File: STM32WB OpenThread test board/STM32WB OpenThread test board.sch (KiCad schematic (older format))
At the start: 0 parts

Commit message: Introduce MCU
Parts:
- added C?: 100n, symbol Device:C_Polarized
- added C? (x8): C, symbol Device:C
- added C?: 100n, symbol Device:C
- added J?: Conn_Coaxial, symbol Connector:Conn_Coaxial
- added L?: L, symbol Device:L
- added SW?: SW_Push, symbol Switch:SW_Push
- added U?: STM32WB15CC, Package_DFN_QFN:QFN-48-1EP_7x7mm_P0.5mm_EP5.6x5.6mm, symbol MCU_ST_STM32WB:STM32WB15CC
- added Y?: 32MHz, symbol Device:Crystal
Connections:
- new net: U?.24 (OSC_OUT), Y?.1
- new net: U?.25 (OSC_IN), Y?.2
- new net: C?.2, L?.2, U?.31 (VFBSMPS)
- new net: L?.1, U?.33 (VLXSMPS)
- new net: C?.1, SW?.2, U?.7 (NRST)
- new net GND: C?.1, C?.2, C?.2, J?.2 (Ext), SW?.1, U?.22 (VSSRF), U?.32 (VSSSMPS), U?.49 (VSS)
- new net VDD: C?.1, U?.1 (VBAT), U?.20 (VDD), U?.23 (VDDRF), U?.34 (VDDSMPS), U?.35 (VDD), U?.40 (VDD), U?.48 (VDD), U?.8 (VDDA)
- no-connect marks 0 -> 2
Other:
- note added: "RF"

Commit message: WIP
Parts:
- added C? (x2): C, symbol Device:C
- added R?: R, symbol Device:R
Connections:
- net GND: now also C?.1, C?.1, C?.1; no longer C?.2
- net VDD: now also R?.1
- net at U?.24 (OSC_OUT): now also Y?.2, C?.2; no longer Y?.1
- net at U?.25 (OSC_IN): now also Y?.1, C?.2; no longer Y?.2
- net at SW?.2, U?.7 (NRST): now also C?.2, R?.2; no longer C?.1
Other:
- moved on the sheet: C?, J?, SW?, Y?
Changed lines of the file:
@@
 L Device:Crystal Y?
 U 1 1 6229DF59
-P 4450 1750
-F 0 "Y?" H 4450 1482 50  0000 C CNN
-F 1 "32MHz" H 4450 1573 50  0000 C CNN
-F 2 "" H 4450 1750 50  0001 C CNN
-F 3 "~" H 4450 1750 50  0001 C CNN
-	1    4450 1750
-	-1   0    0    1
-$EndComp
-Wire Wire Line
-	4600 1800 4950 1800
-Wire Wire Line
-	4950 1900 4300 1900
-Wire Wire Line
-	4600 1800 4600 1750
-Wire Wire Line
-	4300 1750 4300 1900
+P 3850 1550
+F 0 "Y?" H 3850 1282 50  0000 C CNN
+F 1 "32MHz" H 3850 1373 50  0000 C CNN
+F 2 "" H 3850 1550 50  0001 C CNN
+F 3 "~" H 3850 1550 50  0001 C CNN
+	1    3850 1550
+	1    0    0    -1
+$EndComp
 Wire Wire Line
 	5350 1400 5450 1400
@@
 L Connector:Conn_Coaxial J?
 U 1 1 622A9FE4
-P 4000 2100
-F 0 "J?" V 4237 2029 50  0000 C CNN
-F 1 "Conn_Coaxial" V 4146 2029 50  0000 C CNN
-F 2 "" H 4000 2100 50  0001 C CNN
-F 3 " ~" H 4000 2100 50  0001 C CNN
-	1    4000 2100
+P 3150 2100
+F 0 "J?" V 3387 2029 50  0000 C CNN
+F 1 "Conn_Coaxial" V 3296 2029 50  0000 C CNN
+F 2 "" H 3150 2100 50  0001 C CNN
+F 3 " ~" H 3150 2100 50  0001 C CNN
+	1    3150 2100
 	-1   0    0    -1
 $EndComp
@@
 L power:GND #PWR?
 U 1 1 622AEBD7
-P 4000 2300
-F 0 "#PWR?" H 4000 2050 50  0001 C CNN
-F 1 "GND" H 4005 2127 50  0000 C CNN
-F 2 "" H 4000 2300 50  0001 C CNN
-F 3 "" H 4000 2300 50  0001 C CNN
-	1    4000 2300
+P 3150 2300
+F 0 "#PWR?" H 3150 2050 50  0001 C CNN
+F 1 "GND" H 3155 2127 50  0000 C CNN
+F 2 "" H 3150 2300 50  0001 C CNN
+F 3 "" H 3150 2300 50  0001 C CNN
+	1    3150 2300
 	1    0    0    -1
 $EndComp
@@
 L Switch:SW_Push SW?
 U 1 1 622BE53E
-P 4700 1050
-F 0 "SW?" H 4700 1335 50  0000 C CNN
-F 1 "SW_Push" H 4700 1244 50  0000 C CNN
-F 2 "" H 4700 1250 50  0001 C CNN
-F 3 "~" H 4700 1250 50  0001 C CNN
-	1    4700 1050
+P 4700 900
+F 0 "SW?" H 4700 1185 50  0000 C CNN
+F 1 "SW_Push" H 4700 1094 50  0000 C CNN
+F 2 "" H 4700 1100 50  0001 C CNN
+F 3 "~" H 4700 1100 50  0001 C CNN
+	1    4700 900
 	1    0    0    -1
 $EndComp
@@
 L power:GND #PWR?
 U 1 1 622BF9B2
-P 4500 1200
-F 0 "#PWR?" H 4500 950 50  0001 C CNN
-F 1 "GND" V 4505 1072 50  0000 R CNN
-F 2 "" H 4500 1200 50  0001 C CNN
-F 3 "" H 4500 1200 50  0001 C CNN
-	1    4500 1200
+P 4500 1000
+F 0 "#PWR?" H 4500 750 50  0001 C CNN
+F 1 "GND" V 4505 872 50  0000 R CNN
+F 2 "" H 4500 1000 50  0001 C CNN
+F 3 "" H 4500 1000 50  0001 C CNN
+	1    4500 1000
 	0    1    1    0
 $EndComp
-Wire Wire Line
-	4900 1050 4900 1400
+$Comp
+L Device:C C?
+U 1 1 622C3467
+P 4700 1100
+F 0 "C?" V 4448 1100 50  0000 C CNN
+F 1 "100n" V 4539 1100 50  0000 C CNN
+F 2 "" H 4738 950 50  0001 C CNN
+F 3 "~" H 4700 1100 50  0001 C CNN
+	1    4700 1100
+	0    -1   -1   0
+$EndComp
+$Comp
+L power:VDD #PWR?
+U 1 1 622E9133
+P 5200 900
+F 0 "#PWR?" H 5200 750 50  0001 C CNN
+F 1 "VDD" H 5215 1073 50  0000 C CNN
+F 2 "" H 5200 900 50  0001 C CNN
+F 3 "" H 5200 900 50  0001 C CNN
+	1    5200 900
+	0    1    1    0
+$EndComp
+$Comp
+L Device:R R?
+U 1 1 622E9FBF
+P 5050 900
+F 0 "R?" H 5120 946 50  0000 L CNN
+F 1 "R" H 5120 855 50  0000 L CNN
+F 2 "" V 4980 900 50  0001 C CNN
+F 3 "~" H 5050 900 50  0001 C CNN
+	1    5050 900
+	0    1    1    0
+$EndComp
+Wire Wire Line
+	4500 1000 4500 900
+Wire Wire Line
+	4500 1000 4500 1100
+Wire Wire Line
+	4500 1100 4550 1100
+Connection ~ 4500 1000
+Connection ~ 4900 900
+Wire Wire Line
+	4850 1100 4900 1100
+Wire Wire Line
+	4900 1100 4900 900
+Wire Wire Line
+	4900 1100 4900 1600
 Wire Wire Line
 	4900 1600 4950 1600
-$Comp
-L Device:C C?
-U 1 1 622C3467
-P 4700 1400
-F 0 "C?" V 4448 1400 50  0000 C CNN
-F 1 "100n" V 4539 1400 50  0000 C CNN
-F 2 "" H 4738 1250 50  0001 C CNN
-F 3 "~" H 4700 1400 50  0001 C CNN
-	1    4700 1400
-	0    1    1    0
-$EndComp
-Wire Wire Line
-	4850 1400 4900 1400
-Connection ~ 4900 1400
-Wire Wire Line
-	4900 1400 4900 1600
-Wire Wire Line
-	4500 1050 4500 1200
-Wire Wire Line
-	4500 1200 4500 1400
-Wire Wire Line
-	4500 1400 4550 1400
-Connection ~ 4500 1200
+Connection ~ 4900 1100
+$Comp
+L power:GND #PWR?
+U 1 1 62304964
+P 4150 1250
+F 0 "#PWR?" H 4150 1000 50  0001 C CNN
+F 1 "GND" V 4155 1122 50  0000 R CNN
+F 2 "" H 4150 1250 50  0001 C CNN
+F 3 "" H 4150 1250 50  0001 C CNN
+	1    4150 1250
+	-1   0    0    1
+$EndComp
+$Comp
+L power:GND #PWR?
+U 1 1 62304EE0
+P 3500 1250
+F 0 "#PWR?" H 3500 1000 50  0001 C CNN
+F 1 "GND" V 3505 1122 50  0000 R CNN
+F 2 "" H 3500 1250 50  0001 C CNN
+F 3 "" H 3500 1250 50  0001 C CNN
+	1    3500 1250
+	-1   0    0    1
+$EndComp
+Wire Wire Line
+	3700 1550 3500 1550
+Wire Wire Line
+	4000 1550 4150 1550
+$Comp
+L Device:C C?
+U 1 1 6230A174
+P 4150 1400
+F 0 "C?" H 4265 1446 50  0000 L CNN
+F 1 "C" H 4265 1355 50  0000 L CNN
+F 2 "" H 4188 1250 50  0001 C CNN
+F 3 "~" H 4150 1400 50  0001 C CNN
+	1    4150 1400
+	1    0    0    -1
+$EndComp
+$Comp
+L Device:C C?
+U 1 1 6230A550
+P 3500 1400
+F 0 "C?" H 3615 1446 50  0000 L CNN
+F 1 "C" H 3615 1355 50  0000 L CNN
+F 2 "" H 3538 1250 50  0001 C CNN
+F 3 "~" H 3500 1400 50  0001 C CNN
+	1    3500 1400
+	1    0    0    -1
+$EndComp
+Wire Wire Line
+	4950 1800 4150 1800
+Connection ~ 4150 1550
+Wire Wire Line
+	4950 1900 3500 1900
+Connection ~ 3500 1550
+Wire Wire Line
+	4150 1550 4150 1800
+Wire Wire Line
+	3500 1550 3500 1900
 $EndSCHEMATC

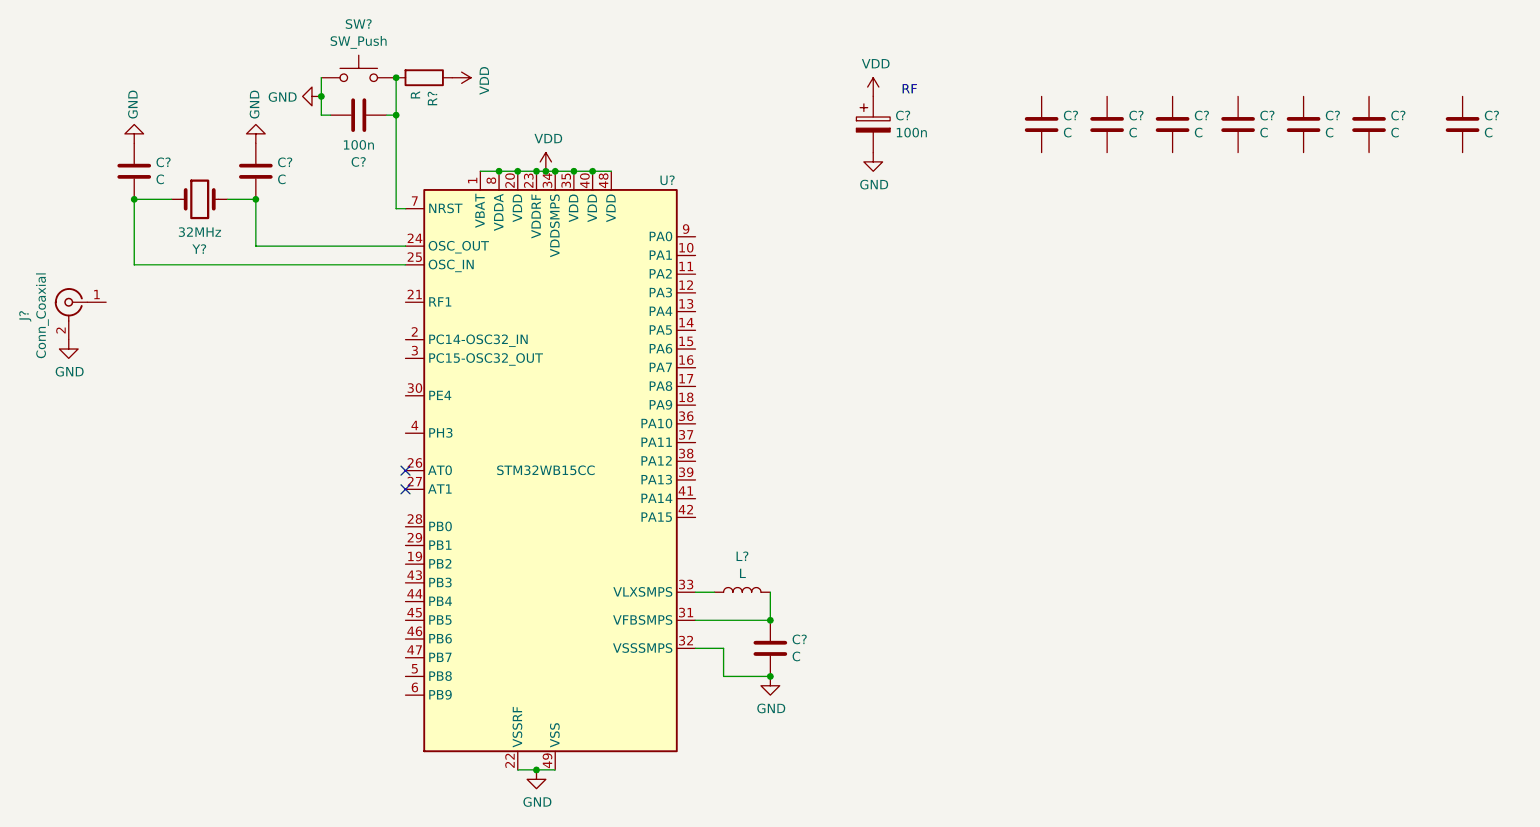
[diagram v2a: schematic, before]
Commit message: WIP: Change STM32WB15 for STM32WB55
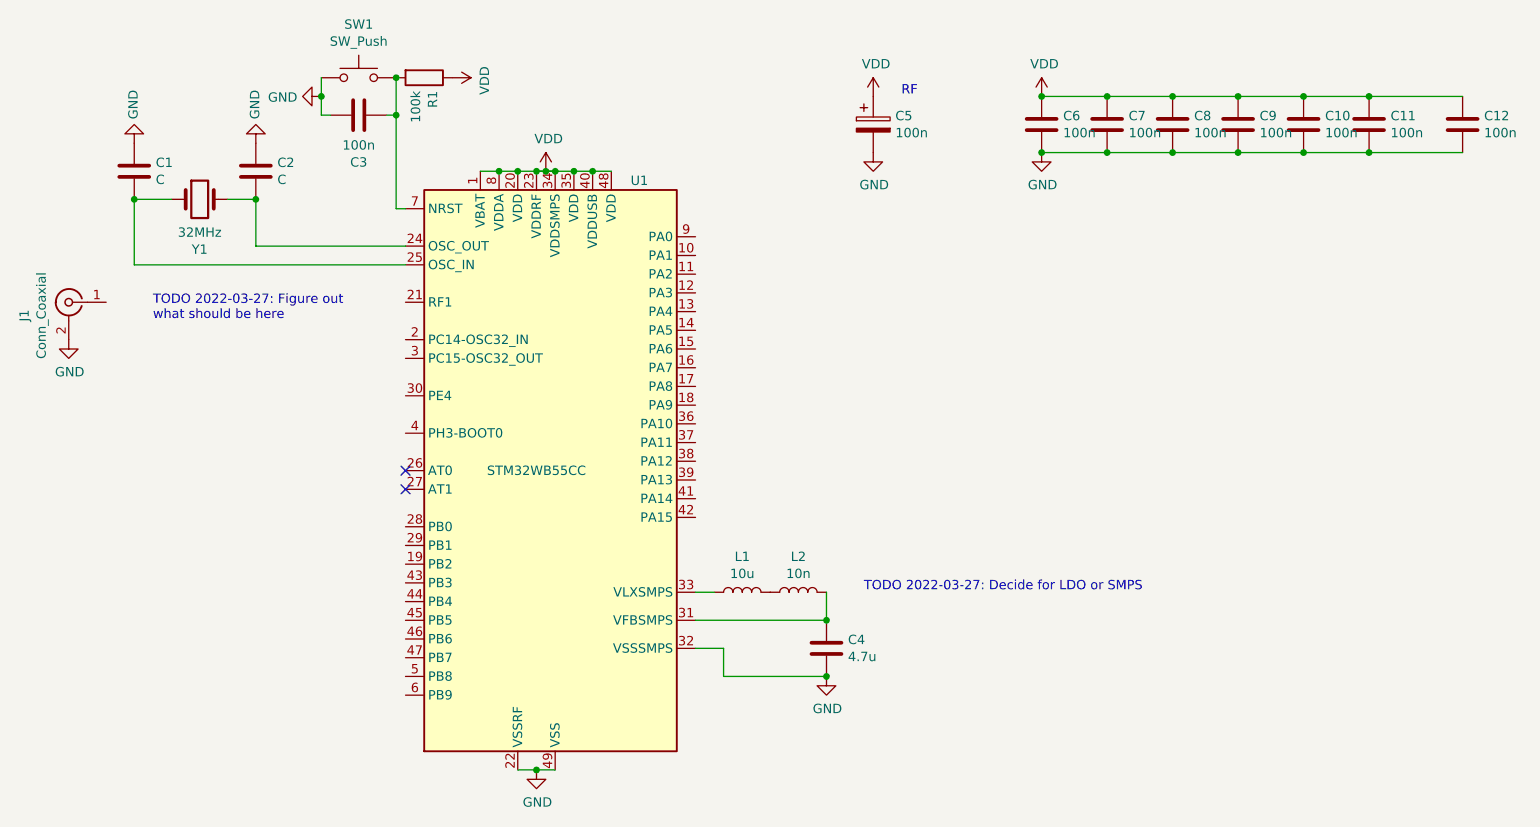
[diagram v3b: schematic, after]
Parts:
- removed U?: STM32WB15CC, Package_DFN_QFN:QFN-48-1EP_7x7mm_P0.5mm_EP5.6x5.6mm, symbol MCU_ST_STM32WB:STM32WB15CC
- added L2: 10n, symbol Device:L
- added U1: STM32WB55CC, Package_DFN_QFN:QFN-48-1EP_7x7mm_P0.5mm_EP5.6x5.6mm, symbol MCU_ST_STM32WB:STM32WB55CC
- C1, C2, C3, C5: renamed from C?; footprint (none) -> Capacitor_SMD:C_0402_1005Metric_Pad0.74x0.62mm_HandSolder
- C10, C11, C12, C6, C7, C8, C9: renamed from C?; value C -> 100n; footprint (none) -> Capacitor_SMD:C_0402_1005Metric_Pad0.74x0.62mm_HandSolder
- C4: renamed from C?; value C -> 4.7u; footprint (none) -> Capacitor_SMD:C_0402_1005Metric_Pad0.74x0.62mm_HandSolder
- J1: renamed from J?; footprint (none) -> Connector_Coaxial:SMA_Amphenol_132203-12_Horizontal
- L1: renamed from L?; value L -> 10u; footprint (none) -> 402 albo 603
- R1: renamed from R?; value R -> 100k; footprint (none) -> Resistor_SMD:R_0402_1005Metric_Pad0.72x0.64mm_HandSolder
- gave numbers to parts that had none: 2
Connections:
- net GND: now also C10.2, C11.2, C12.2, C6.2, C7.2, C8.2, C9.2, U1.22 (VSSRF), U1.32 (VSSSMPS), U1.49 (VSS)
- net VDD: now also C10.1, C11.1, C12.1, C6.1, C7.1, C8.1, C9.1, U1.1 (VBAT), U1.20 (VDD), U1.23 (VDDRF), U1.34 (VDDSMPS), U1.35 (VDD), U1.40 (VDDUSB), U1.48 (VDD), U1.8 (VDDA)
- net at C2.2, Y1.2: now also U1.24 (OSC_OUT)
- net at C1.2, Y1.1: now also U1.25 (OSC_IN)
- net at C4.2: now also L2.2, U1.31 (VFBSMPS); no longer L1.2
- net at L1.1: now also U1.33 (VLXSMPS)
- net at C3.2, R1.2, SW1.2: now also U1.7 (NRST)
- new net: L1.2, L2.1
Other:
- note added: "TODO 2022-03-27: Decide for LDO or SMPS"
- note added: "TODO 2022-03-27: Figure out\nwhat should be here"
- moved on the sheet: C4

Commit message: WIP
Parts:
- J1: footprint Connector_Coaxial:SMA_Amphenol_132203-12_Horizontal -> Connector_Coaxial:U.FL_Hirose_U.FL-R-SMT-1_Vertical
- SW1: value SW_Push -> C&K KMR421NG LFS
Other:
- note added: "Think about Capacitor-Coil-Capacitor"
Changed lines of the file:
@@
 Sheet 1 1
 Title "STM32WB OpenThread Test Board"
-Date "2022-03-05"
-Rev "v0.0.1"
+Date "2022-04-03"
+Rev "v0.1.0"
 Comp "Sergiusz Warga"
 Comment1 ""
@@
 F 0 "J1" V 3387 2029 50  0000 C CNN
 F 1 "Conn_Coaxial" V 3296 2029 50  0000 C CNN
-F 2 "Connector_Coaxial:SMA_Amphenol_132203-12_Horizontal" H 3150 2100 50  0001 C CNN
+F 2 "Connector_Coaxial:U.FL_Hirose_U.FL-R-SMT-1_Vertical" H 3150 2100 50  0001 C CNN
 F 3 " ~" H 3150 2100 50  0001 C CNN
 	1    3150 2100
@@
 P 4700 900
 F 0 "SW1" H 4700 1185 50  0000 C CNN
-F 1 "SW_Push" H 4700 1094 50  0000 C CNN
+F 1 "C&K KMR421NG LFS" H 4700 1094 50  0000 C CNN
 F 2 "" H 4700 1100 50  0001 C CNN
-F 3 "~" H 4700 1100 50  0001 C CNN
+F 3 "https://www.tme.eu/Document/82270d8c9e16493c80bcc1a437fbde29/KMR2_series_DTE.pdf" H 4700 1100 50  0001 C CNN
 	1    4700 900
 	1    0    0    -1
@@
 Wire Wire Line
 	5350 1400 5450 1400
-Wire Wire Line
-	5700 1400 5750 1400
 Connection ~ 5950 1400
 Connection ~ 5450 1400
@@
 	5550 1400 5650 1400
 Connection ~ 5650 1400
-Wire Wire Line
-	5650 1400 5700 1400
 Connection ~ 5750 1400
 Wire Wire Line
@@
 Wire Wire Line
 	5850 1400 5950 1400
+Text Notes 3350 2350 0    50   ~ 0
+Think about Capacitor-Coil-Capacitor
 $EndSCHEMATC
